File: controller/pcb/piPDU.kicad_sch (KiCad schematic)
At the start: 36 parts, among them J0 SCR_BTN1, J1 SCR_LED1, J10 SCR_BTN6, J11 SCR_LED6, J12 SCR_BTN7, J13 SCR_LED7, J14 SCR_BTN8, J15 SCR_LED8, J16 SCR_BTN9, J17 SCR_LED9, J18 SCR_BTN10, J19 SCR_LED10, J2 SCR_BTN2, J20 SCR_BTN11, J21 SCR_LED11, J22 SCR_BTN12, J23 SCR_LED12, J24 SCR_BTN13, J25 SCR_LED13, J26 SCR_BTN14, J27 SCR_LED14, J28 SCR_BTN15, J29 SCR_LED15, J3 SCR_LED2, J30 SCR_BTN16, J31 SCR_LED16, J32 SCR_5V, J33 SCR_LCD_PWR, J34 SCR_LCD_DATA, J35 Raspberry_Pi_2_3, J4 SCR_BTN3, J5 SCR_LED3, J6 SCR_BTN4, J7 SCR_LED4, J8 SCR_BTN5, J9 SCR_LED5

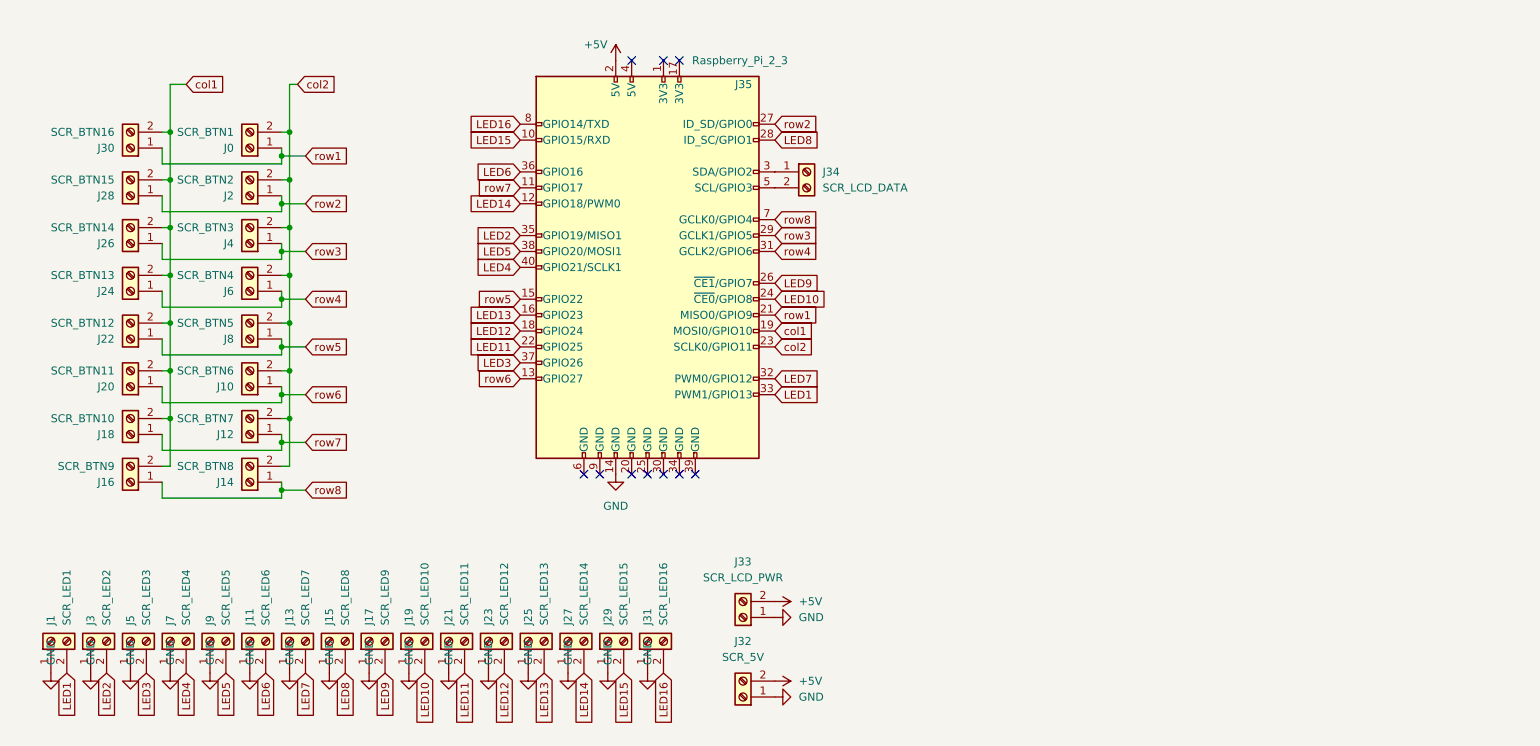
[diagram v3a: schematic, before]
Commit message: Update controller PCB and schematic to use GPIO expanders
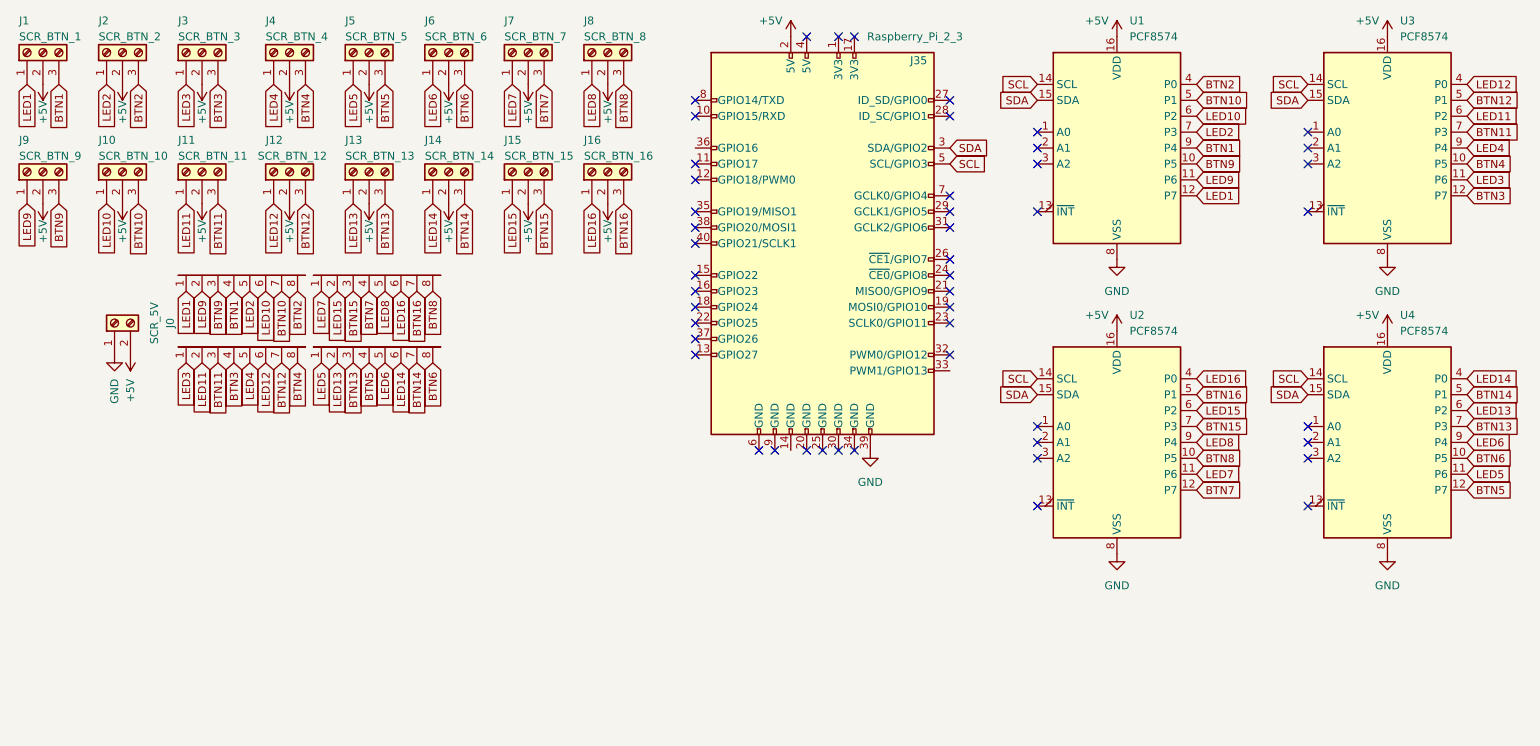
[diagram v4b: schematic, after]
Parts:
- removed J0: SCR_BTN1, TerminalBlock:TerminalBlock_bornier-2_P5.08mm, symbol Connector:Screw_Terminal_01x02
- removed J1: SCR_LED1, TerminalBlock:TerminalBlock_bornier-2_P5.08mm, symbol Connector:Screw_Terminal_01x02
- removed J10: SCR_BTN6, TerminalBlock:TerminalBlock_bornier-2_P5.08mm, symbol Connector:Screw_Terminal_01x02
- removed J11: SCR_LED6, TerminalBlock:TerminalBlock_bornier-2_P5.08mm, symbol Connector:Screw_Terminal_01x02
- removed J12: SCR_BTN7, TerminalBlock:TerminalBlock_bornier-2_P5.08mm, symbol Connector:Screw_Terminal_01x02
- removed J13: SCR_LED7, TerminalBlock:TerminalBlock_bornier-2_P5.08mm, symbol Connector:Screw_Terminal_01x02
- removed J14: SCR_BTN8, TerminalBlock:TerminalBlock_bornier-2_P5.08mm, symbol Connector:Screw_Terminal_01x02
- removed J15: SCR_LED8, TerminalBlock:TerminalBlock_bornier-2_P5.08mm, symbol Connector:Screw_Terminal_01x02
- removed J16: SCR_BTN9, TerminalBlock:TerminalBlock_bornier-2_P5.08mm, symbol Connector:Screw_Terminal_01x02
- removed J17: SCR_LED9, TerminalBlock:TerminalBlock_bornier-2_P5.08mm, symbol Connector:Screw_Terminal_01x02
- removed J18: SCR_BTN10, TerminalBlock:TerminalBlock_bornier-2_P5.08mm, symbol Connector:Screw_Terminal_01x02
- removed J19: SCR_LED10, TerminalBlock:TerminalBlock_bornier-2_P5.08mm, symbol Connector:Screw_Terminal_01x02
- removed J2: SCR_BTN2, TerminalBlock:TerminalBlock_bornier-2_P5.08mm, symbol Connector:Screw_Terminal_01x02
- removed J20: SCR_BTN11, TerminalBlock:TerminalBlock_bornier-2_P5.08mm, symbol Connector:Screw_Terminal_01x02
- removed J21: SCR_LED11, TerminalBlock:TerminalBlock_bornier-2_P5.08mm, symbol Connector:Screw_Terminal_01x02
- removed J22: SCR_BTN12, TerminalBlock:TerminalBlock_bornier-2_P5.08mm, symbol Connector:Screw_Terminal_01x02
- removed J23: SCR_LED12, TerminalBlock:TerminalBlock_bornier-2_P5.08mm, symbol Connector:Screw_Terminal_01x02
- removed J24: SCR_BTN13, TerminalBlock:TerminalBlock_bornier-2_P5.08mm, symbol Connector:Screw_Terminal_01x02
- removed J25: SCR_LED13, TerminalBlock:TerminalBlock_bornier-2_P5.08mm, symbol Connector:Screw_Terminal_01x02
- removed J26: SCR_BTN14, TerminalBlock:TerminalBlock_bornier-2_P5.08mm, symbol Connector:Screw_Terminal_01x02
- removed J27: SCR_LED14, TerminalBlock:TerminalBlock_bornier-2_P5.08mm, symbol Connector:Screw_Terminal_01x02
- removed J28: SCR_BTN15, TerminalBlock:TerminalBlock_bornier-2_P5.08mm, symbol Connector:Screw_Terminal_01x02
- removed J29: SCR_LED15, TerminalBlock:TerminalBlock_bornier-2_P5.08mm, symbol Connector:Screw_Terminal_01x02
- removed J3: SCR_LED2, TerminalBlock:TerminalBlock_bornier-2_P5.08mm, symbol Connector:Screw_Terminal_01x02
- removed J30: SCR_BTN16, TerminalBlock:TerminalBlock_bornier-2_P5.08mm, symbol Connector:Screw_Terminal_01x02
- removed J31: SCR_LED16, TerminalBlock:TerminalBlock_bornier-2_P5.08mm, symbol Connector:Screw_Terminal_01x02
- removed J33: SCR_LCD_PWR, TerminalBlock:TerminalBlock_bornier-2_P5.08mm, symbol Connector:Screw_Terminal_01x02
- removed J34: SCR_LCD_DATA, TerminalBlock:TerminalBlock_bornier-2_P5.08mm, symbol Connector:Screw_Terminal_01x02
- removed J4: SCR_BTN3, TerminalBlock:TerminalBlock_bornier-2_P5.08mm, symbol Connector:Screw_Terminal_01x02
- removed J5: SCR_LED3, TerminalBlock:TerminalBlock_bornier-2_P5.08mm, symbol Connector:Screw_Terminal_01x02
- removed J6: SCR_BTN4, TerminalBlock:TerminalBlock_bornier-2_P5.08mm, symbol Connector:Screw_Terminal_01x02
- removed J7: SCR_LED4, TerminalBlock:TerminalBlock_bornier-2_P5.08mm, symbol Connector:Screw_Terminal_01x02
- removed J8: SCR_BTN5, TerminalBlock:TerminalBlock_bornier-2_P5.08mm, symbol Connector:Screw_Terminal_01x02
- removed J9: SCR_LED5, TerminalBlock:TerminalBlock_bornier-2_P5.08mm, symbol Connector:Screw_Terminal_01x02
- added J1: SCR_BTN_1, TerminalBlock:TerminalBlock_bornier-3_P5.08mm, symbol Connector:Screw_Terminal_01x03
- added J10: SCR_BTN_10, TerminalBlock:TerminalBlock_bornier-3_P5.08mm, symbol Connector:Screw_Terminal_01x03
- added J11: SCR_BTN_11, TerminalBlock:TerminalBlock_bornier-3_P5.08mm, symbol Connector:Screw_Terminal_01x03
- added J12: SCR_BTN_12, TerminalBlock:TerminalBlock_bornier-3_P5.08mm, symbol Connector:Screw_Terminal_01x03
- added J13: SCR_BTN_13, TerminalBlock:TerminalBlock_bornier-3_P5.08mm, symbol Connector:Screw_Terminal_01x03
- added J14: SCR_BTN_14, TerminalBlock:TerminalBlock_bornier-3_P5.08mm, symbol Connector:Screw_Terminal_01x03
- added J15: SCR_BTN_15, TerminalBlock:TerminalBlock_bornier-3_P5.08mm, symbol Connector:Screw_Terminal_01x03
- added J16: SCR_BTN_16, TerminalBlock:TerminalBlock_bornier-3_P5.08mm, symbol Connector:Screw_Terminal_01x03
- added J2: SCR_BTN_2, TerminalBlock:TerminalBlock_bornier-3_P5.08mm, symbol Connector:Screw_Terminal_01x03
- added J3: SCR_BTN_3, TerminalBlock:TerminalBlock_bornier-3_P5.08mm, symbol Connector:Screw_Terminal_01x03
- added J4: SCR_BTN_4, TerminalBlock:TerminalBlock_bornier-3_P5.08mm, symbol Connector:Screw_Terminal_01x03
- added J5: SCR_BTN_5, TerminalBlock:TerminalBlock_bornier-3_P5.08mm, symbol Connector:Screw_Terminal_01x03
- added J6: SCR_BTN_6, TerminalBlock:TerminalBlock_bornier-3_P5.08mm, symbol Connector:Screw_Terminal_01x03
- added J7: SCR_BTN_7, TerminalBlock:TerminalBlock_bornier-3_P5.08mm, symbol Connector:Screw_Terminal_01x03
- added J8: SCR_BTN_8, TerminalBlock:TerminalBlock_bornier-3_P5.08mm, symbol Connector:Screw_Terminal_01x03
- added J9: SCR_BTN_9, TerminalBlock:TerminalBlock_bornier-3_P5.08mm, symbol Connector:Screw_Terminal_01x03
- added U1, U2, U3, U4: PCF8574, Custom:PCF8574, symbol Interface_Expansion:PCF8574
- added U5, U6, U7, U8: 8P_Header, Connector_PinHeader_2.54mm:PinHeader_1x08_P2.54mm_Vertical, symbol Custom:8P_Header
- renumbered J32 to J0
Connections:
- net +5V: now also J1.2 (Pin_2), J10.2 (Pin_2), J11.2 (Pin_2), J12.2 (Pin_2), J13.2 (Pin_2), J14.2 (Pin_2), J15.2 (Pin_2), J16.2 (Pin_2), J2.2 (Pin_2), J3.2 (Pin_2), J4.2 (Pin_2), J5.2 (Pin_2), J6.2 (Pin_2), J7.2 (Pin_2), J8.2 (Pin_2), J9.2 (Pin_2), U1.16 (VDD), U2.16 (VDD), U3.16 (VDD), U4.16 (VDD)
- net GND: now also J35.39 (GND), U1.8 (VSS), U2.8 (VSS), U3.8 (VSS), U4.8 (VSS); no longer J35.14 (GND)
- net LED1: now also J1.1 (Pin_1), U1.12 (P7), U5.1; no longer J35.33 (PWM1/GPIO13)
- net LED10: now also J10.1 (Pin_1), U1.6 (P2), U5.6; no longer J35.24 (~{CE0}/GPIO8)
- net LED11: now also J11.1 (Pin_1), U3.6 (P2), U6.2; no longer J35.22 (GPIO25)
- net LED12: now also J12.1 (Pin_1), U3.4 (P0), U6.6; no longer J35.18 (GPIO24)
- net LED13: now also J13.1 (Pin_1), U4.6 (P2), U8.2; no longer J35.16 (GPIO23)
- net LED14: now also J14.1 (Pin_1), U4.4 (P0), U8.6; no longer J35.12 (GPIO18/PWM0)
- net LED15: now also J15.1 (Pin_1), U2.6 (P2), U7.2; no longer J35.10 (GPIO15/RXD)
- net LED16: now also J16.1 (Pin_1), U2.4 (P0), U7.6; no longer J35.8 (GPIO14/TXD)
- net LED2: now also J2.1 (Pin_1), U1.7 (P3), U5.5; no longer J35.35 (GPIO19/MISO1)
- net LED3: now also J3.1 (Pin_1), U3.11 (P6), U6.1; no longer J35.37 (GPIO26)
- net LED4: now also J4.1 (Pin_1), U3.9 (P4), U6.5; no longer J35.40 (GPIO21/SCLK1)
- net LED5: now also J5.1 (Pin_1), U4.11 (P6), U8.1; no longer J35.38 (GPIO20/MOSI1)
- net LED6: now also J6.1 (Pin_1), U4.9 (P4), U8.5; no longer J35.36 (GPIO16)
- net LED7: now also J7.1 (Pin_1), U2.11 (P6), U7.1; no longer J35.32 (PWM0/GPIO12)
- net LED8: now also J8.1 (Pin_1), U2.9 (P4), U7.5; no longer J35.28 (ID_SC/GPIO1)
- net LED9: now also J9.1 (Pin_1), U1.11 (P6), U5.2; no longer J35.26 (~{CE1}/GPIO7)
- net SDA: now reaches J35.3 (SDA/GPIO2)
- net SDA: now also U1.15 (SDA), U2.15 (SDA), U3.15 (SDA), U4.15 (SDA)
- net SCL: now reaches J35.5 (SCL/GPIO3)
- net SCL: now also U1.14 (SCL), U2.14 (SCL), U3.14 (SCL), U4.14 (SCL)
- net col1: no longer names the net of J35.19 (MOSI0/GPIO10)
- net col2: no longer names the net of J35.23 (SCLK0/GPIO11)
- net row1: no longer names the net of J35.21 (MISO0/GPIO9)
- net row2: no longer names the net of J35.27 (ID_SD/GPIO0)
- net row3: no longer names the net of J35.29 (GCLK1/GPIO5)
- net row4: no longer names the net of J35.31 (GCLK2/GPIO6)
- net row5: no longer names the net of J35.15 (GPIO22)
- net row6: no longer names the net of J35.13 (GPIO27)
- net row7: no longer names the net of J35.11 (GPIO17)
- net row8: no longer names the net of J35.7 (GCLK0/GPIO4)
- new net BTN1: J1.3 (Pin_3), U1.9 (P4), U5.4
- new net BTN10: J10.3 (Pin_3), U1.5 (P1), U5.7
- new net BTN11: J11.3 (Pin_3), U3.7 (P3), U6.3
- new net BTN12: J12.3 (Pin_3), U3.5 (P1), U6.7
- new net BTN13: J13.3 (Pin_3), U4.7 (P3), U8.3
- new net BTN14: J14.3 (Pin_3), U4.5 (P1), U8.7
- new net BTN15: J15.3 (Pin_3), U2.7 (P3), U7.3
- new net BTN16: J16.3 (Pin_3), U2.5 (P1), U7.7
- new net BTN2: J2.3 (Pin_3), U1.4 (P0), U5.8
- new net BTN3: J3.3 (Pin_3), U3.12 (P7), U6.4
- new net BTN4: J4.3 (Pin_3), U3.10 (P5), U6.8
- new net BTN5: J5.3 (Pin_3), U4.12 (P7), U8.4
- new net BTN6: J6.3 (Pin_3), U4.10 (P5), U8.8
- new net BTN7: J7.3 (Pin_3), U2.12 (P7), U7.4
- new net BTN8: J8.3 (Pin_3), U2.10 (P5), U7.8
- new net BTN9: J9.3 (Pin_3), U1.10 (P5), U5.3
- no-connect marks 10 -> 49
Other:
- moved on the sheet: J0, J35
